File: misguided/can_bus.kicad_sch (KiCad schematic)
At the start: 0 parts

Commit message: buncha stuff
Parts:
- added C301: C_Small, symbol Device:C_Small
- added R301, R302, R303, R304: 33, symbol Device:R
- added U301: MCP2518FDT-E/SLVAO, SOIC14_SL_MCH, symbol misguided:MCP2518FDT-E_SLVAO
- added Y301: Crystal_GND24_Small, symbol Device:Crystal_GND24_Small
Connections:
- new net: R302.1, U301.11 (SDI)
- new net: R303.1, U301.10 (SCK)
- new net: R301.1, U301.12 (SDO)
- new net: R304.1, U301.4 (*INT)
- new net +5V: C301.2, U301.14 (VDD)
- new net CLK: R303.2
- new net GND: C301.1, U301.7 (VSS)
- new net INT: R304.2
- new net MISO: R301.2
- new net MOSI: R302.2
- no-connect marks 0 -> 3

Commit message: more setup
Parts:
- removed Y301: Crystal_GND24_Small, symbol Device:Crystal_GND24_Small
- added C302, C303: 100nf, Capacitor_SMD:C_0402_1005Metric, symbol Device:C_Small
- added U302: TCAN1044VDDFR, misguided:SOT-23-THIN-8_DDF_TEX, symbol misguided:TCAN1044VDDFR
- C301: value C_Small -> 100nf; footprint (none) -> Capacitor_SMD:C_0402_1005Metric
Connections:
- net +5V: now also C303.2, U302.3 (VCC); no longer C301.2, U301.14 (VDD)
- net CAN_H: now also U302.7 (CANH)
- net CAN_L: now also U302.6 (CANL)
- net GND: now also C302.1, C303.1, U302.2 (GND), U302.8 (STB)
- net tx: now reaches U301.1 (TXCAN)
- net tx: now also U302.1 (TXD)
- net rx: now reaches U301.2 (RXCAN)
- net rx: now also U302.4 (RXD)
- new net +3.3V: C301.2, C302.2, U301.14 (VDD), U302.5 (VIO)

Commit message: various fixes
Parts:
- removed R302, R303: 33, symbol Device:R
- added C304: 100nf, Capacitor_SMD:C_0402_1005Metric, symbol Device:C_Small
- added R305: 0, symbol Device:R
- added U303: 40Mhz, Oscillator:Oscillator_SMD_Abracon_ASE-4Pin_3.2x2.5mm, symbol misguided:OT2EL4C4JI-111OLP-40M
- U301: footprint SOIC14_SL_MCH -> misguided:SOIC14_SL_MCH
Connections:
- net +3.3V: now also C304.2, R305.2, U303.4 (VDD)
- net CLK: now also U301.10 (SCK)
- net GND: now also C304.1, U303.2 (GND)
- net MOSI: now also U301.11 (SDI)
- net ~{CS}: now reaches U301.13 (NCS)
- net at U301.6 (OSC1): now also U303.4 (VDD)
- new net: R305.1, U303.1 (OE)
- no-connect marks 3 -> 4

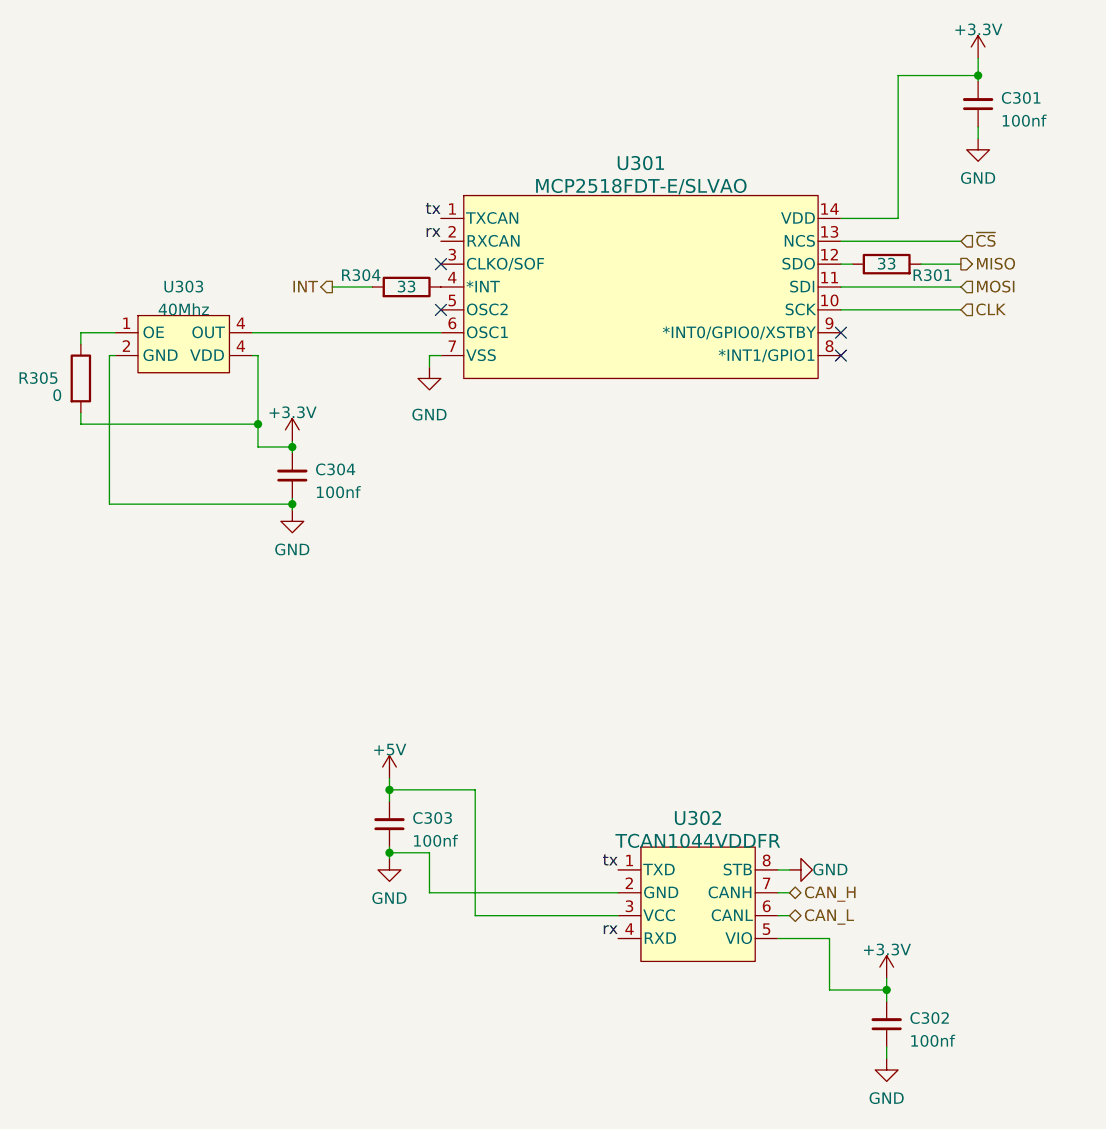
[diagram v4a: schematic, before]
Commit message: fixed schematic associations
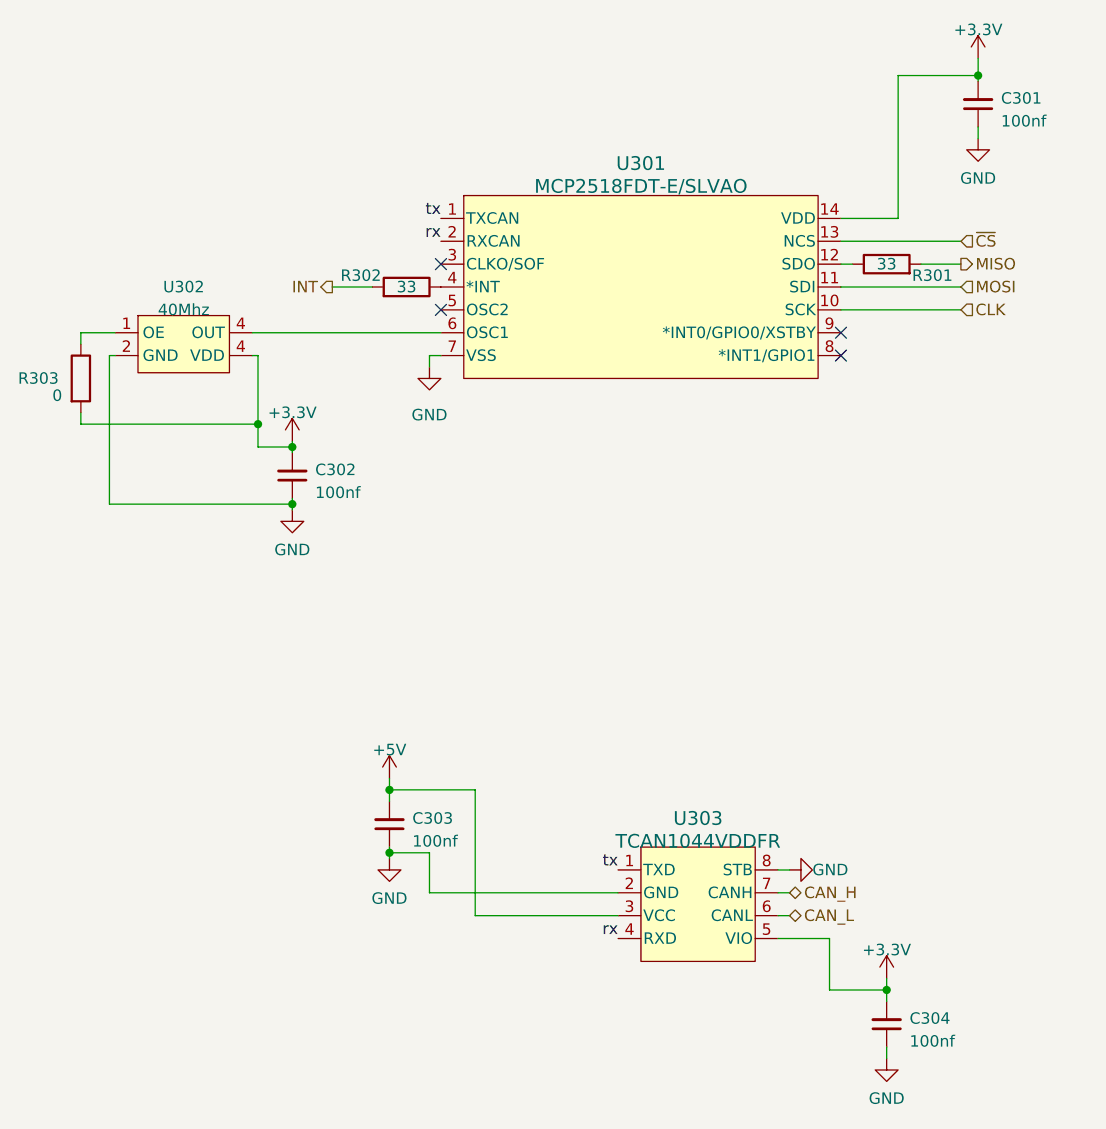
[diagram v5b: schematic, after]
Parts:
- R301: footprint (none) -> Resistor_SMD:R_0402_1005Metric
- R302: renamed from R304; footprint (none) -> Resistor_SMD:R_0402_1005Metric
- R303: renamed from R305; footprint (none) -> Resistor_SMD:R_0402_1005Metric
- renumbered C304 to C302, C302 to C304, U303 to U302, U302 to U303

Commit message: layed out and ordered
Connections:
- net at U301.6 (OSC1): now also U302.3 (OUT); no longer U302.4 (VDD)
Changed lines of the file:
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@@
-    (stroke (width 0) (type default))
-  )
-  (wire (pts (xy 117.475 153.035) (xy 118.745 153.035))
     (stroke (width 0) (type default))
   )
@@
     (stroke (width 0) (type default))
   )
+  (wire (pts (xy 117.475 150.495) (xy 127 150.495))
+    (stroke (width 0) (type default))
+  )
   (wire (pts (xy 40.005 89.535) (xy 40.005 88.265))
     (stroke (width 0) (type default))
@@
     (stroke (width 0) (type default))
   )
+  (wire (pts (xy 117.475 153.035) (xy 127 153.035))
+    (stroke (width 0) (type default))
+  )
   (wire (pts (xy 117.475 147.955) (xy 118.745 147.955))
     (stroke (width 0) (type default))
@@
   )
   (wire (pts (xy 129.54 161.29) (xy 129.54 162.56))
-    (stroke (width 0) (type default))
-  )
-  (wire (pts (xy 117.475 150.495) (xy 118.745 150.495))
     (stroke (width 0) (type default))
   )
@@
     (effects (font (size 1.27 1.27)) (justify right bottom))
   )
+  (label "can_N" (at 121.285 153.035 0) (fields_autoplaced)
+    (effects (font (size 1.27 1.27)) (justify left bottom))
+  )
+  (label "can_P" (at 121.285 150.495 0) (fields_autoplaced)
+    (effects (font (size 1.27 1.27)) (justify left bottom))
+  )
   (hierarchical_label "MISO" (shape output) (at 137.795 80.645 0) (fields_autoplaced)
     (effects (font (size 1.27 1.27)) (justify left))
@@
     (effects (font (size 1.27 1.27)) (justify right))
   )
-  (hierarchical_label "CAN_L" (shape bidirectional) (at 118.745 153.035 0) (fields_autoplaced)
+  (hierarchical_label "CAN_L" (shape bidirectional) (at 127 153.035 0) (fields_autoplaced)
     (effects (font (size 1.27 1.27)) (justify left))
   )
@@
     (effects (font (size 1.27 1.27)) (justify left))
   )
-  (hierarchical_label "CAN_H" (shape bidirectional) (at 118.745 150.495 0) (fields_autoplaced)
+  (hierarchical_label "CAN_H" (shape bidirectional) (at 127 150.495 0) (fields_autoplaced)
     (effects (font (size 1.27 1.27)) (justify left))
   )
@@
   (symbol (lib_id "misguided:MCP2518FDT-E_SLVAO") (at 102.235 73.025 0) (unit 1)
     (in_bom yes) (on_board yes) (dnp no) (fields_autoplaced)
-    (property "Reference" "U301" (at 102.235 69.469 0)
+    (property "Reference" "U301" (at 102.235 69.85 0)
       (effects (font (size 1.524 1.524)))
     )
-    (property "Value" "MCP2518FDT-E/SLVAO" (at 102.235 72.009 0)
+    (property "Value" "MCP2518FDT-E/SLVAO" (at 102.235 72.39 0)
       (effects (font (size 1.524 1.524)))
     )
@@
     (pin "1")
     (pin "2")
+    (pin "3")
     (pin "4")
-    (pin "4")
-    (instances
+    (instances
